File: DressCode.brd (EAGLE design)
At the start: 43.8 x 36.2 mm, 44 parts, among them M1 MIC9.7MM, M2 MIC6MM, Q1 2N7002, Q2 2N7002, Q3 2N7002, SW1 PCM12SMTR, U1 MCP6S21, U2 MCP6S21, U3 MCP6G02, U4 PIC24FV32KA304-I/PT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

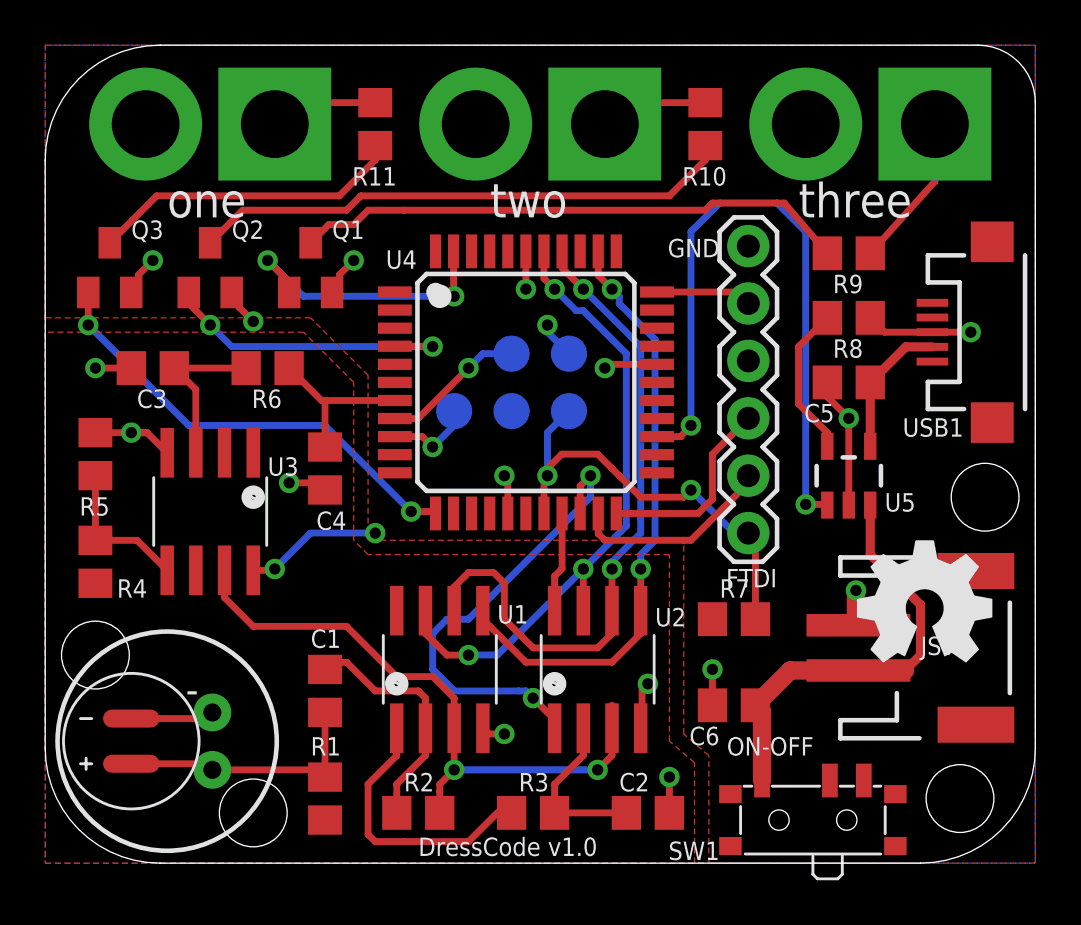
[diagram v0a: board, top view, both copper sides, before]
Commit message: Fix USB connection error
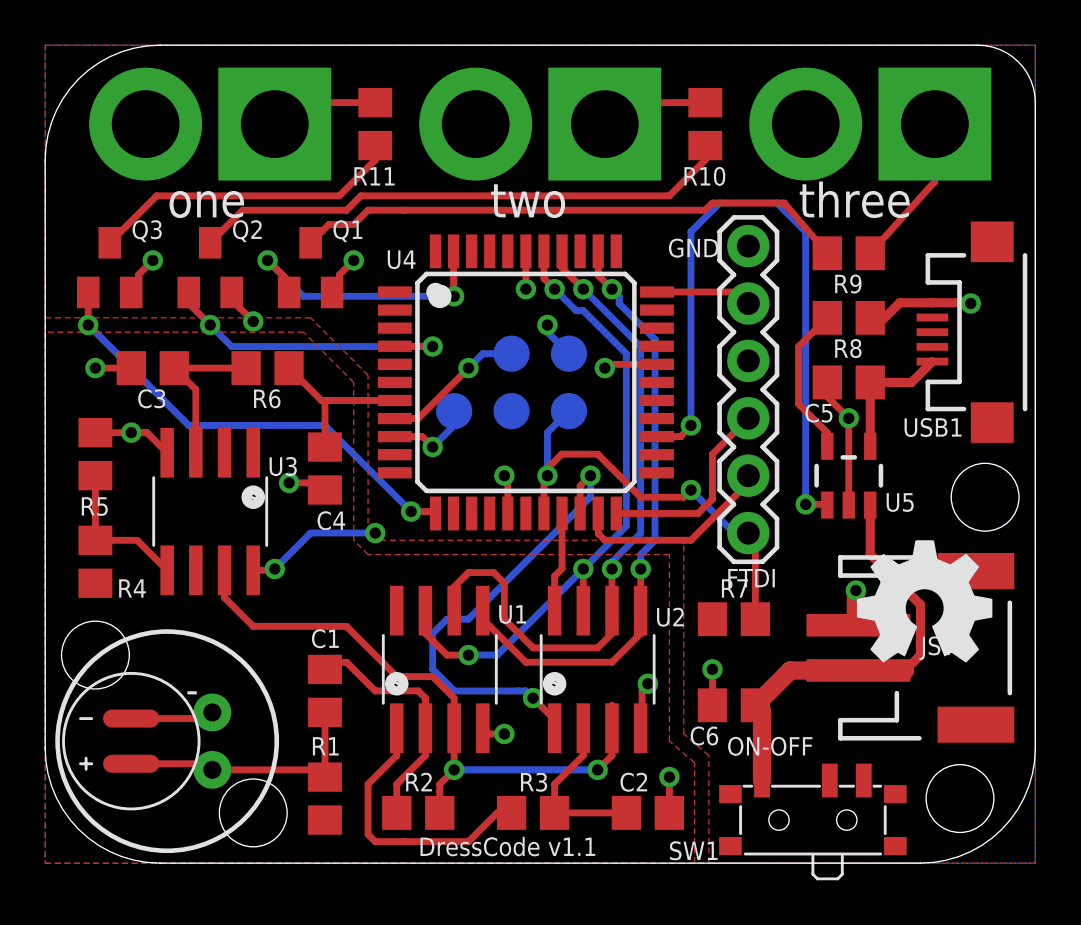
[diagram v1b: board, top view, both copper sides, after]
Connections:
- net GND: now also USB1.GND; no longer USB1.D+
- net USB1: now also USB1.VBUS; no longer USB1.D-
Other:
- board text added: "DressCode v1.1"
- board text removed: "DressCode v1.0"
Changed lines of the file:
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@@
 <hole x="2.2225" y="9.2075" drill="3"/>
 <hole x="9.2075" y="2.2225" drill="3"/>
-<text x="16.51" y="0.3175" size="0.8128" layer="121" font="vector">DressCode v1.0</text>
+<text x="16.51" y="0.3175" size="0.8128" layer="121" font="vector">DressCode v1.1</text>
 <text x="41.91" y="5.3975" size="0.8128" layer="122" font="vector" rot="MR0">Seb Madgwick</text>
-<text x="41.91" y="6.985" size="0.8128" layer="122" font="vector" rot="MR0">DressCode v1.0</text>
+<text x="41.91" y="6.985" size="0.8128" layer="122" font="vector" rot="MR0">DressCode v1.1</text>
 <circle x="17.4625" y="25.0825" radius="0.3175" width="0.4064" layer="121"/>
 <circle x="15.5575" y="7.9375" radius="0.3175" width="0.4064" layer="121"/>
@@
 <wire x1="12.3825" y1="16.5125" x2="12.0675" y2="16.8275" width="0.3048" layer="1"/>
 <wire x1="12.0675" y1="16.8275" x2="10.795" y2="16.8275" width="0.3048" layer="1"/>
-<contactref element="USB1" pad="D+"/>
 <contactref element="C5" pad="1"/>
 <contactref element="U5" pad="2"/>
@@
 <wire x1="27.0725" y1="22.0725" x2="24.93" y2="22.0725" width="0.3048" layer="1"/>
 <wire x1="24.93" y1="22.0725" x2="24.765" y2="21.9075" width="0.3048" layer="1" curve="90"/>
-<via x="40.9575" y="23.495" extent="1-16" drill="0.5"/>
 <via x="35.8775" y="12.065" extent="1-16" drill="0.5"/>
-<wire x1="39.26" y1="23.495" x2="40.9575" y2="23.495" width="0.3048" layer="1"/>
 <via x="29.5275" y="8.5725" extent="1-16" drill="0.5"/>
 <wire x1="29.53" y1="6.985" x2="29.845" y2="6.985" width="0.3048" layer="1"/>
@@
 <wire x1="8.5725" y1="25.5725" x2="8.5725" y2="24.60625" width="0.3048" layer="1"/>
 <wire x1="8.5725" y1="24.60625" x2="9.2075" y2="23.97125" width="0.3048" layer="1"/>
-<wire x1="39.26" y1="23.495" x2="37.145" y2="23.495" width="0.3048" layer="1"/>
-<wire x1="37.145" y1="23.495" x2="36.51" y2="24.13" width="0.3048" layer="1"/>
 <wire x1="26.4125" y1="6.0325" x2="26.4125" y2="7.68" width="0.3048" layer="1"/>
 <wire x1="26.4125" y1="7.68" x2="26.67" y2="7.9375" width="0.3048" layer="1"/>
@@
 <wire x1="13.0175" y1="25.5725" x2="13.0175" y2="26.035" width="0.3048" layer="1"/>
 <wire x1="13.0175" y1="26.035" x2="13.6525" y2="26.67" width="0.3048" layer="1"/>
+<contactref element="USB1" pad="GND"/>
+<via x="40.9575" y="24.765" extent="1-16" drill="0.5"/>
+<wire x1="39.26" y1="24.795" x2="40.9575" y2="24.795" width="0.4064" layer="1"/>
+<wire x1="40.9575" y1="24.795" x2="40.9575" y2="24.765" width="0.4064" layer="1"/>
+<wire x1="39.26" y1="24.795" x2="37.8125" y2="24.795" width="0.4064" layer="1"/>
+<wire x1="37.8125" y1="24.795" x2="36.83" y2="23.8125" width="0.4064" layer="1"/>
+<wire x1="36.83" y1="23.8125" x2="36.8275" y2="23.8125" width="0.4064" layer="1"/>
+<wire x1="36.8275" y1="23.8125" x2="36.51" y2="24.13" width="0.4064" layer="1"/>
 </signal>
 <signal name="AVDD">
@@
 </signal>
 <signal name="USB1">
-<contactref element="USB1" pad="D-"/>
 <contactref element="U5" pad="4"/>
 <contactref element="C5" pad="2"/>
 <wire x1="36.51" y1="21.2725" x2="36.51" y2="18.4451" width="0.4064" layer="1"/>
-<wire x1="39.26" y1="22.845" x2="38.0825" y2="22.845" width="0.4064" layer="1"/>
-<wire x1="38.0825" y1="22.845" x2="36.51" y2="21.2725" width="0.4064" layer="1"/>
+<contactref element="USB1" pad="VBUS"/>
+<wire x1="36.51" y1="21.2725" x2="38.3375" y2="21.2725" width="0.4064" layer="1"/>
+<wire x1="38.3375" y1="21.2725" x2="39.26" y2="22.195" width="0.4064" layer="1"/>
 </signal>
 <signal name="N$15">
